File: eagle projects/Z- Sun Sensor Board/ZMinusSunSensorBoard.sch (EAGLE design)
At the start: 194 parts, among them J2 HIROSE_FH19C-6S-0.5SH(10), J3 HIROSE_FH19C-6S-0.5SH(10), J4 HIROSE_FH19C-6S-0.5SH(10), J5 HIROSE_FH19C-6S-0.5SH(10), U1 ADS7841E_2K5, U13 ADS7841E_2K5, U15 TLV9051IDCKR, U19 TLV9051IDCKR, U2 ADS7841E_2K5, U21 TLV9051IDCKR, U23 TLV9051IDCKR, U24 TLV9051IDCKR, U25 ADS7841E_2K5, U26 TLV9051IDCKR, U27 ADS7841E_2K5, U28 TLV9051IDCKR, U29 TLV9051IDCKR, U3 TLV9051IDCKR, U30 TLV9051IDCKR, U31 TLV9051IDCKR, U32 TLV9051IDCKR, U4 LM20BIM7X_NOPB, U6 TLV9051IDCKR, U8 TLV9051IDCKR, U9 TLV9051IDCKR

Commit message: Rev B almost ready
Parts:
- removed A1: XY_SUN_SENSOR, my_library:XY_SUN_SENSOR
- removed C104, C107, C109, C112, C114, C69, C86, C97: 0.1u, resistor:C-EUC0402
- removed C105, C110, C111, C115, C116, C54, C70, C84, C98: 0.022u, resistor:C-EUC0402
- removed C106, C108, C113, C55, C68, C85, C99: 4.7u, resistor:C-EUC0402
- removed J4, J5: HIROSE_FH19C-6S-0.5SH(10), my_library:HIROSE_FH19C-6S-0.5SH(10)
- removed JP1: (no value), pinhead:PINHD-1X2
- removed JP3: (no value), pinhead:PINHD-2X5
- removed R2: 0R, rcl:R-US_R0805
- removed R28, R57, R63, R69: 13.7k, resistor:R-US_R0402
- removed R31, R46, R55, R61, R67: 3.74k, resistor:R-US_R0402
- removed R56, R62, R68: 280R, resistor:R-US_R0402
- removed TP12, TP18, TP20, TP7, TP8: TESTPOINT, my_library:TESTPOINT
- removed U15, U24, U28, U30, U31, U32: TLV9051IDCKR, my_library:TLV9051IDCKR
- added C10, C17, C24, C36, C39, C58, C64, C7: 0.1u, resistor:C-EUC0402
- added C11, C18, C34, C37, C40, C59, C8: 0.022u, resistor:C-EUC0402
- added C13, C23, C35, C38, C44, C57, C6, C63, C9: 4.7u, rcl:C-EUC0805
- added C2: 0.1u, rcl:C-EUC0402
- added J1: TE-1734829-2, my_library:TE-1734829-2
- added JP2, JP4, JP5, JP6: (no value), my_library:PINHD-1X6_MTG_HOLES_MTG
- added R27: 5.1M, rcl:R-US_R0402
- added R30, R37, R43, R49, R71, R79: 280R, resistor:R-US_R0402
- added R35, R41, R72, R74, R80: 13.7k, resistor:R-US_R0402
- added R36, R42, R73, R75, R81: 3.74k, resistor:R-US_R0402
- added TP23, TP24, TP25, TP27, TP29: TESTPOINT, my_library:TESTPOINT
- added U$1: SSR_MOUNT_03, my_library:SSR_MOUNT_03
- added U10, U11, U12, U14, U16, U17: TSV991AILT, my_library:TSV991AILT
- added U5: LM20BIM7X_NOPB, my_library:LM20BIM7X_NOPB
- C100, C71: value 0.022u -> 4.7u; device resistor:C-EUC0402 -> rcl:C-EUC0805
- C101, C27, C32: value 0.022u -> 0.1u
- C103, C96: value 4.7u -> 0.022u
- C25, C28: value 4.7u -> 0.022u; device rcl:C-EUC0805 -> resistor:C-EUC0402
- C26, C29: value 0.1u -> 4.7u; device resistor:C-EUC0402 -> rcl:C-EUC0805
- C52, C82: value 4.7u -> 0.1u
- C53, C67, C83: value 0.1u -> 0.022u
- C87: device resistor:C-EUC0402 -> rcl:C-EUC0805
- J2: value HIROSE_FH19C-6S-0.5SH(10) -> (none); device my_library:HIROSE_FH19C-6S-0.5SH(10) -> my_library:PINHD-2X5_MTG_HOLES
- J3: value HIROSE_FH19C-6S-0.5SH(10) -> (none); device my_library:HIROSE_FH19C-6S-0.5SH(10) -> my_library:HDR_1X2_
- LED1: device led:LEDCHIP-LED0603 -> led:LEDCHIPLED-0603-TTW
- R14, R25: value 280R -> 5.1M; device resistor:R-US_R0402 -> rcl:R-US_R0402
- R15: value 13.7k -> 5.1M; device resistor:R-US_R0402 -> rcl:R-US_R0402
- R17: device resistor:R-US_R0402 -> rcl:R-US_R0402
- R19: value 3.74k -> 5.1M; device resistor:R-US_R0402 -> rcl:R-US_R0402
- R44, R53, R59, R65: value 280R -> 13.7k
- R45, R54, R60, R66: value 13.7k -> 3.74k
- R58, R64, R70: value 3.74k -> 280R
- U19, U21, U23, U26, U29, U3, U6, U8, U9: value TLV9051IDCKR -> TSV991AILT; device my_library:TLV9051IDCKR -> my_library:TSV991AILT
- renumbered C30 to C3, C31 to C4, C33 to C5
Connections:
- removed net !CS!_SUN_Z+: U2.!CS
- removed net N$1: R2.1, U4.VO
- removed net N$13: R14.2, R15.1, U9.+
- removed net N$3: A1G$2.C1, C27.1, R7.1, U6.-
- removed net N$31: R22.2, R23.1, U3.+
- removed net N$34: R25.2, R28.1, U23.+
- removed net N$36: R32.2, R33.1, U24.+
- removed net N$45: R44.2, R45.1, U19.+
- removed net N$47: R50.2, R51.1, U21.+
- removed net N$5: TP17.TP, U25.CH0
- removed net N$56: R56.2, R57.1, U28.+
- removed net N$58: R59.2, R60.1, U29.+
- removed net N$64: R65.2, R66.1, U31.+
- removed net N$66: R68.2, R69.1, U32.+
- removed net N$68: JP3.10
- removed net N$9: R8.2, R9.1, U8.+
- removed net TEMP: R2.2, TP1.TP, U2.CH0
- new net N$20: R27.1, U5.NC
- new net N$27: C8.1, R13.1, U$1G$2.C2, U8.IN-
- new net N$28: R8.2, R9.1, U8.IN+
- new net N$30: R43.2, R44.1, U12.IN+
- new net N$32: R22.2, R23.1, U3.IN+
- new net N$40: R30.2, R35.1, U9.IN+
- new net N$42: C18.1, R42.1, U$1G$2.C1, U11.IN-
- new net N$43: R37.2, R41.1, U11.IN+
- new net N$60: R49.2, R53.1, U14.IN+
- new net N$69: R64.2, R65.1, U23.IN+
- new net N$71: R71.2, R72.1, U17.IN+
- new net N$74: R70.2, R74.1, U26.IN+
- new net N$78: R79.2, R80.1, U29.IN+
- new net TEMP_EXT: TP17.TP, U25.CH0, U5.VO
- new net TEMP_INT: TP1.TP, U2.CH0, U4.VO
- net !CS!_SUN_X+: now also J2.2; no longer JP3.2
- net !CS!_SUN_X-: now also J2.7; no longer JP3.7
- net !CS!_SUN_Y+: now also J2.4; no longer JP3.4
- net !CS!_SUN_Y-: now also J2.9; no longer JP3.9
- net !CS!_SUN_Z-: now also J2.6, U2.!CS; no longer JP3.6
- net +3V3: now also C10.1, C100.1, C101.1, C13.1, C17.1, C2.1, C23.1, C24.1, C27.1, C32.1, C35.1, C36.1, C38.1, C39.1, C44.1, C57.1, C58.1, C6.1, C63.1, C64.1, C7.1, C71.1, C9.1, J1.3V3, J2.10, J3.1, R35.2, R41.2, R44.2, R53.2, R59.2, R65.2, R72.2, R74.2, R80.2, U10.VCC, U11.VCC, U12.VCC, U14.VCC, U16.VCC, U17.VCC, U19.VCC, U21.VCC, U23.VCC, U26.VCC, U29.VCC, U3.VCC, U5.V+, U6.VCC, U8.VCC, U9.VCC; no longer C103.1, C104.1, C106.1, C107.1, C108.1, C109.1, C112.1, C113.1, C114.1, C25.1, C28.1, C53.1, C55.1, C67.1, C68.1, C69.1, C83.1, C85.1, C86.1, C96.1, C97.1, C99.1, JP1.1, R15.2, R28.2, R45.2, R54.2, R57.2, R60.2, R63.2, R66.2, R69.2, U15.V+, U19.V+, U21.V+, U23.V+, U24.V+, U26.V+, U28.V+, U29.V+, U3.V+, U30.V+, U31.V+, U32.V+, U6.V+, U8.V+, U9.V+
- net 0_DEGREES: now also C18.2, R42.2, TP24.TP, U11.OUT; no longer C27.2, R7.2, TP3.TP, U6.OUT
- net 120_DEGREES: now also C8.2; no longer C32.2
- net 240_DEGREES: now also R7.2, TP3.TP, U6.OUT; no longer R19.2, TP8.TP, U9.OUT
- net GND: now also C10.2, C100.2, C101.2, C13.2, C17.2, C2.2, C23.2, C24.2, C27.2, C32.2, C35.2, C36.2, C38.2, C39.2, C44.2, C57.2, C58.2, C6.2, C63.2, C64.2, C7.2, C71.2, C9.2, J1.GND, JP2.2, JP2.4, JP2.6, JP4.2, JP4.4, JP4.6, JP5.2, JP5.4, JP5.6, JP6.2, JP6.4, JP6.6, R15.1, R19.1, R25.2, R27.2, R30.1, R37.1, R43.1, R49.1, R58.1, R64.1, R70.1, R71.1, R79.1, U$1G$2.A1, U$1G$2.A2, U$1G$2.A3, U10.VSS, U11.VSS, U12.VSS, U14.VSS, U16.VSS, U17.VSS, U19.VSS, U21.VSS, U23.VSS, U26.VSS, U29.VSS, U3.VSS, U5.GND_1, U5.GND_2, U6.VSS, U8.VSS, U9.VSS; no longer A1G$2.A1, A1G$2.A2, A1G$2.A3, C103.2, C104.2, C106.2, C107.2, C108.2, C109.2, C112.2, C113.2, C114.2, C25.2, C28.2, C53.2, C55.2, C67.2, C68.2, C69.2, C83.2, C85.2, C86.2, C96.2, C97.2, C99.2, J2.2, J2.4, J2.6, J2.MTGTAB1, J2.MTGTAB2, J3.4, J3.6, J3.MTGTAB1, J3.MTGTAB2, J4.2, J4.4, J4.6, J4.MTGTAB1, J4.MTGTAB2, J5.2, J5.4, J5.6, J5.MTGTAB1, J5.MTGTAB2, JP1.2, R25.1, R44.1, R53.1, R56.1, R59.1, R62.1, R65.1, R68.1, U15.V-, U19.V-, U21.V-, U23.V-, U24.V-, U26.V-, U28.V-, U29.V-, U3.V-, U30.V-, U31.V-, U32.V-, U6.V-, U8.V-, U9.V-
- net N$10: now also R15.2
- net N$11: now also R14.2
- net N$12: now also R7.1, U$1G$2.C3, U6.IN-; no longer A1G$2.C3, R19.1, U9.-
- net N$14: now also R19.2
- net N$23: now also C96.1, JP6.3, R75.1, U26.IN-; no longer C100.1, J5.3, R31.1, U23.-
- net N$29: now also C83.1, JP6.1, R66.1, U23.IN-; no longer C84.1, J5.1, R24.1, U3.-
- net N$35: now also C103.1, JP6.5, R81.1, U29.IN-; no longer C101.1, J5.5, R34.1, U24.-
- net N$37: now also C34.1, JP5.1, R45.1, U12.IN-; no longer C98.1, J4.1, R64.1, U30.-
- net N$38: now also C25.1, JP4.1, U10.IN-; no longer C54.1, J3.1, U15.-
- net N$41: now also R32.2, R33.1, U16.IN+; no longer R38.2, R39.1, U15.+
- net N$44: now also C40.1, JP4.3, R24.1, U3.IN-; no longer C70.1, J3.3, R46.1, U19.-
- net N$46: now also C53.1, JP4.5, R34.1, U16.IN-; no longer C71.1, J3.5, R52.1, U21.-
- net N$49: now also C11.1, JP2.1, R36.1, U9.IN-; no longer C105.1, J2.1, R55.1, U26.-
- net N$54: now also R50.2, R51.1, U19.IN+; no longer R53.2, R54.1, U26.+
- net N$55: now also C28.1, JP2.3, R54.1, U14.IN-; no longer C110.1, J2.3, R58.1, U28.-
- net N$57: now also C37.1, JP2.5, R73.1, U17.IN-; no longer C111.1, J2.5, R61.1, U29.-
- net N$6: now also R38.2, R39.1, U10.IN+; no longer R1.2, R3.1, U6.+
- net N$61: now also R58.2, R59.1, U21.IN+; no longer R62.2, R63.1, U30.+
- net N$63: now also C59.1, JP5.3, R52.1, U19.IN-; no longer C115.1, J4.3, R67.1, U31.-
- net N$65: now also C67.1, JP5.5, R60.1, U21.IN-; no longer C116.1, J4.5, R70.1, U32.-
- net N$67: now also J2.8, R25.1; no longer JP3.8
- net N$8: now also R1.2, R3.1, U6.IN+; no longer A1G$2.C2, C32.1, R13.1, U8.-
- net UCB0_SPI_CLK: now also J2.5; no longer JP3.5
- net UCB0_SPI_MISO: now also J2.1; no longer JP3.1
- net UCB0_SPI_MOSI: now also J2.3; no longer JP3.3
- net X+_0_DEGREES: now also C11.2, R36.2, U9.OUT; no longer C105.2, R55.2, U26.OUT
- net X+_120_DEGREES: now also C28.2, R54.2, TP16.TP, U14.OUT; no longer C110.2, R58.2, TP15.TP, U28.OUT
- net X+_240_DEGREES: now also C37.2, R73.2, TP25.TP, U17.OUT; no longer C111.2, R61.2, TP16.TP, U29.OUT
- net X-_0_DEGREES: now also C25.2, U10.OUT; no longer C54.2, U15.OUT
- net X-_120_DEGREES: now also C40.2, R24.2, TP5.TP, U3.OUT; no longer C70.2, R46.2, TP11.TP, U19.OUT
- net X-_240_DEGREES: now also C53.2, R34.2, TP9.TP, U16.OUT; no longer C71.2, R52.2, TP12.TP, U21.OUT
- net Y+_0_DEGREES: now also C34.2, R45.2, TP11.TP, U12.OUT; no longer C98.2, R64.2, TP18.TP, U30.OUT
- net Y+_120_DEGREES: now also C59.2, R52.2, TP15.TP, U19.OUT; no longer C115.2, R67.2, TP19.TP, U31.OUT
- net Y+_240_DEGREES: now also C67.2, R60.2, TP19.TP, U21.OUT; no longer C116.2, R70.2, TP20.TP, U32.OUT
- net Y-_0_DEGREES: now also C103.2, R81.2, TP29.TP, U29.OUT; no longer C84.2, R24.2, TP5.TP, U3.OUT
- net Y-_120_DEGREES: now also C96.2, R75.2, TP27.TP, U26.OUT; no longer C100.2, R31.2, TP7.TP, U23.OUT
- net Y-_240_DEGREES: now also C83.2, R66.2, TP23.TP, U23.OUT; no longer C101.2, R34.2, TP9.TP, U24.OUT
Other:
- note removed: "Custom machine sun sensor mount for Z- face photodiodes mechanically to board"

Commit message: I thinks its done
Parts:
- JP2, JP4, JP5, JP6: device my_library:PINHD-1X6_MTG_HOLES_MTG -> my_library:PINHD-2X3_MTG_HOLESHOLES
- LED1: device led:LEDCHIPLED-0603-TTW -> led:LEDCHIP-LED0603
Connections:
- net GND: now also JP2.1, JP2.3, JP2.5, JP4.1, JP4.3, JP4.5, JP5.1, JP5.3, JP5.5, JP6.1, JP6.3, JP6.5; no longer JP2.2, JP2.4, JP2.6, JP4.2, JP4.4, JP4.6, JP5.2, JP5.4, JP5.6, JP6.2, JP6.4, JP6.6
- net N$23: now also JP6.4; no longer JP6.3
- net N$29: now also JP6.6; no longer JP6.1
- net N$35: now also JP6.2; no longer JP6.5
- net N$37: now also JP5.2; no longer JP5.1
- net N$38: now also JP4.2; no longer JP4.1
- net N$44: now also JP4.4; no longer JP4.3
- net N$46: now also JP4.6; no longer JP4.5
- net N$49: now also JP2.2; no longer JP2.1
- net N$55: now also JP2.4; no longer JP2.3
- net N$57: now also JP2.6; no longer JP2.5
- net N$63: now also JP5.4; no longer JP5.3
- net N$65: now also JP5.6; no longer JP5.5
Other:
- note added: "ADCS Electrical"
- note added: "B"
- note added: "Temperature Sensors"
- note removed: "A"
- moved on the sheet: JP2, JP4, JP5, JP6

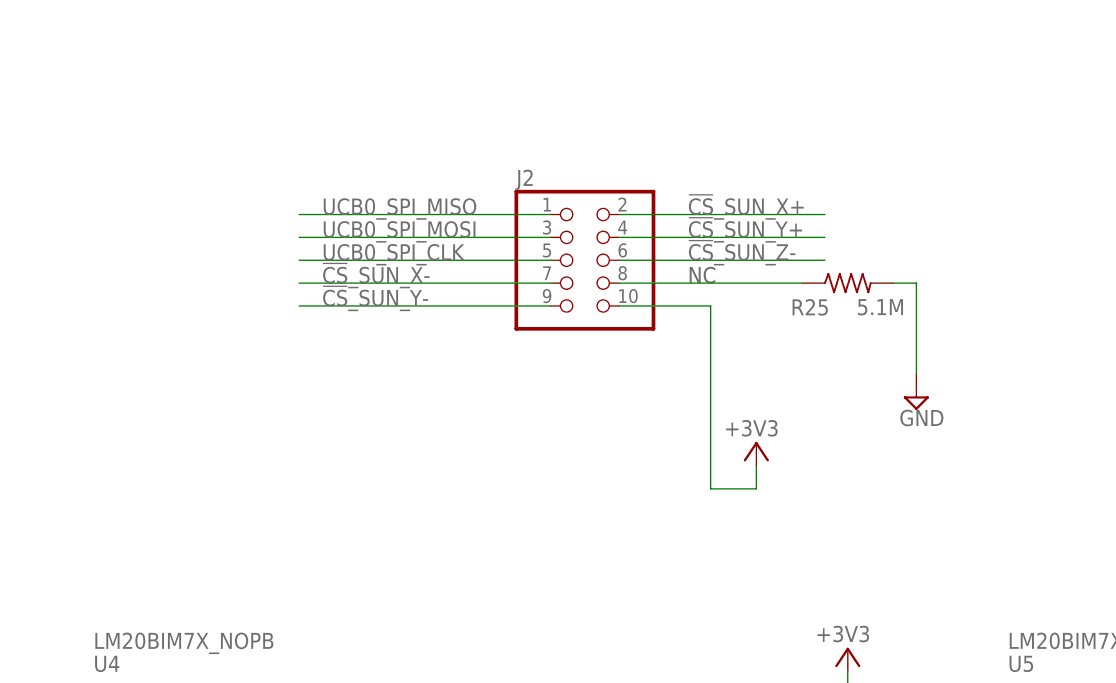
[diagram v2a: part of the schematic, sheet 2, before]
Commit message: Changed most connector changes of Z- board
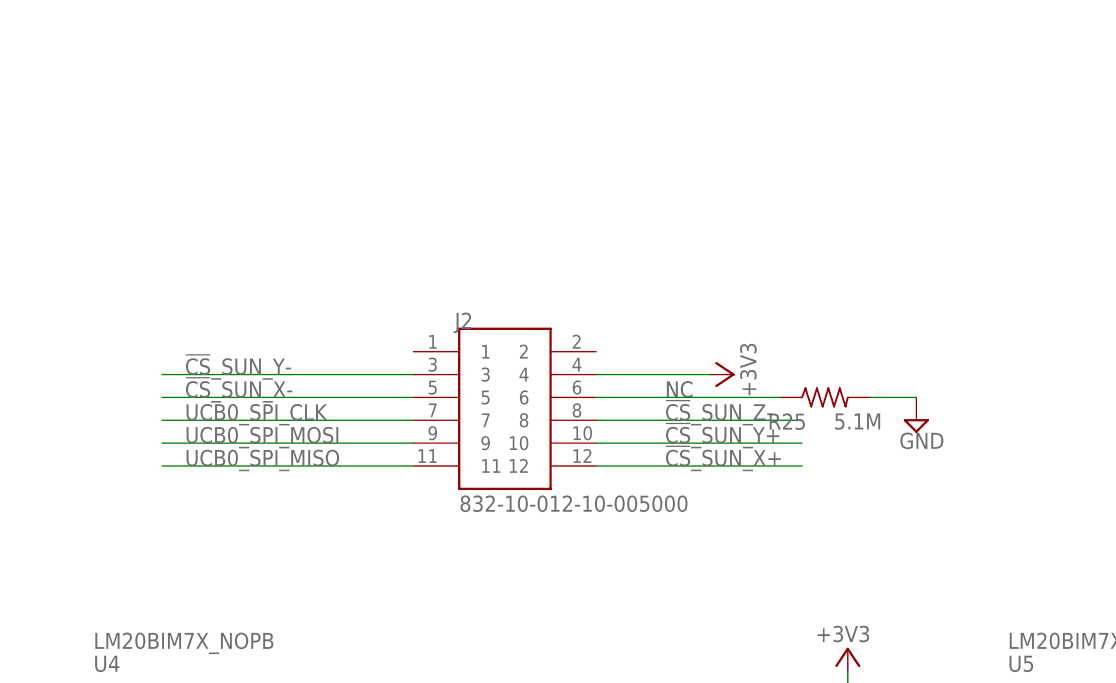
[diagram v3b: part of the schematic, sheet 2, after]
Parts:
- removed JP2, JP4, JP5, JP6: (no value), my_library:PINHD-2X3_MTG_HOLESHOLES
- added J4, J5, J6, J7: 830-10-006-20-005000, 830-10-006-20-005000:830-10-006-20-005000
- J2: value (none) -> 832-10-012-10-005000; device my_library:PINHD-2X5_MTG_HOLES -> 832-10-012-10-005000:832-10-012-10-005000
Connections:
- removed net N$23: C96.1, JP6.4, R75.1, U26.IN-
- removed net N$35: C103.1, JP6.2, R81.1, U29.IN-
- removed net N$37: C34.1, JP5.2, R45.1, U12.IN-
- removed net N$63: C59.1, JP5.4, R52.1, U19.IN-
- new net N$13: C96.1, J7.3, R75.1, U26.IN-
- new net N$17: C103.1, J7.5, R81.1, U29.IN-
- new net N$3: C34.1, J6.5, R45.1, U12.IN-
- new net N$5: C59.1, J6.3, R52.1, U19.IN-
- net !CS!_SUN_X+: now also J2.12; no longer J2.2
- net !CS!_SUN_X-: now also J2.5; no longer J2.7
- net !CS!_SUN_Y+: now also J2.10; no longer J2.4
- net !CS!_SUN_Y-: now also J2.3; no longer J2.9
- net !CS!_SUN_Z-: now also J2.8; no longer J2.6
- net +3V3: now also J2.4; no longer J2.10
- net GND: now also J4.2, J4.4, J4.6, J5.2, J5.4, J5.6, J6.2, J6.4, J6.6, J7.2, J7.4, J7.6; no longer JP2.1, JP2.3, JP2.5, JP4.1, JP4.3, JP4.5, JP5.1, JP5.3, JP5.5, JP6.1, JP6.3, JP6.5
- net N$29: now also J7.1; no longer JP6.6
- net N$38: now also J4.5; no longer JP4.2
- net N$44: now also J4.3; no longer JP4.4
- net N$46: now also J4.1; no longer JP4.6
- net N$49: now also J5.5; no longer JP2.2
- net N$55: now also J5.3; no longer JP2.4
- net N$57: now also J5.1; no longer JP2.6
- net N$65: now also J6.1; no longer JP5.6
- net N$67: now also J2.6; no longer J2.8
- net UCB0_SPI_CLK: now also J2.7; no longer J2.5
- net UCB0_SPI_MISO: now also J2.11; no longer J2.1
- net UCB0_SPI_MOSI: now also J2.9; no longer J2.3
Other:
- moved on the sheet: R25

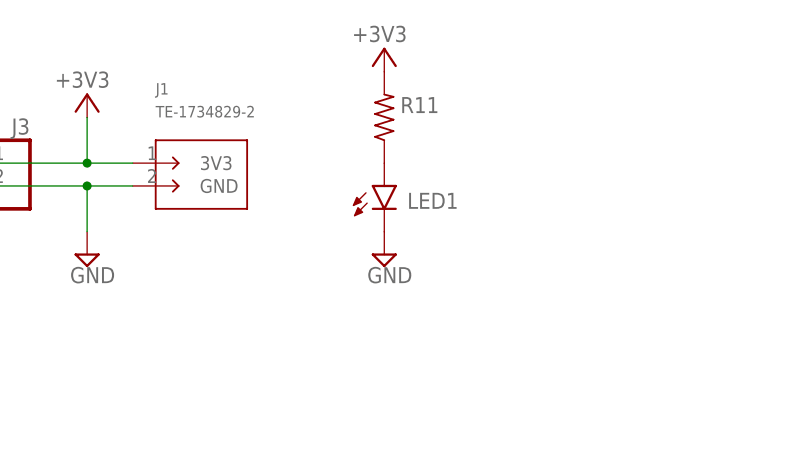
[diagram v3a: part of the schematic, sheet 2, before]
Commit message: Removed LED to Z-
Removed a voltage testing LED and associated resistor from the Z- board, BOM was updated accordingly.
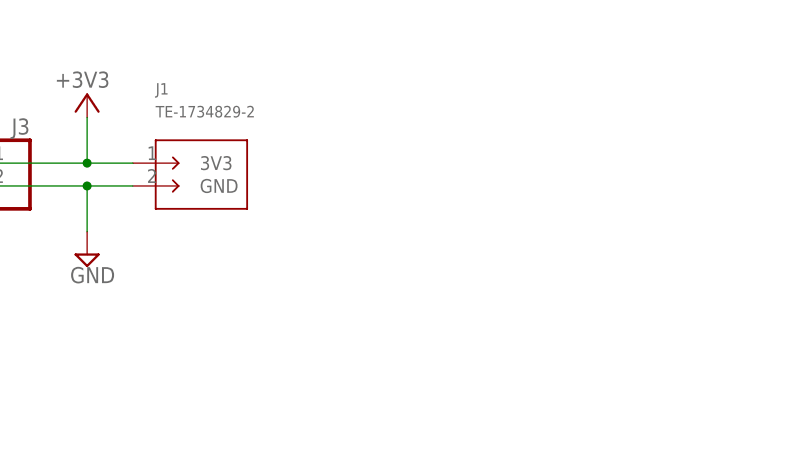
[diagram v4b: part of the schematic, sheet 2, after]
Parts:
- removed LED1: (no value), led:LEDCHIP-LED0603
- removed R11: (no value), rcl:R-US_R0603
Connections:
- removed net N$21: LED1.A, R11.1
- net +3V3: no longer R11.2
- net GND: no longer LED1.C
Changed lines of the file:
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@@
 <part name="J1" library="my_library" library_urn="urn:adsk.eagle:library:22876504" deviceset="TE-1734829-2" device="" package3d_urn="urn:adsk.eagle:package:27602902/2"/>
 <part name="J3" library="my_library" library_urn="urn:adsk.eagle:library:22876504" deviceset="HDR_1X2" device="_" package3d_urn="urn:adsk.eagle:package:24527019/1"/>
-<part name="R11" library="rcl" library_urn="urn:adsk.eagle:library:334" deviceset="R-US_" device="R0603" package3d_urn="urn:adsk.eagle:package:23555/3"/>
-<part name="LED1" library="led" library_urn="urn:adsk.eagle:library:259" deviceset="LED" device="CHIP-LED0603" package3d_urn="urn:adsk.eagle:package:15819/3"/>
-<part name="+3V22" library="supply1" library_urn="urn:adsk.eagle:library:371" deviceset="+3V3" device=""/>
-<part name="SUPPLY1" library="supply2" library_urn="urn:adsk.eagle:library:372" deviceset="GND" device=""/>
 <part name="+3V23" library="supply1" library_urn="urn:adsk.eagle:library:371" deviceset="+3V3" device=""/>
 <part name="SUPPLY9" library="supply2" library_urn="urn:adsk.eagle:library:372" deviceset="GND" device=""/>
@@
 <attribute name="VALUE" x="105.41" y="167.64" size="1.778" layer="96" rot="MR0"/>
 </instance>
-<instance part="R11" gate="G$1" x="144.78" y="180.34" smashed="yes" rot="R90">
-<attribute name="NAME" x="146.558" y="180.8226" size="1.778" layer="95"/>
-<attribute name="VALUE" x="148.082" y="176.53" size="1.778" layer="96" rot="R90"/>
-</instance>
-<instance part="LED1" gate="G$1" x="144.78" y="172.72" smashed="yes">
-<attribute name="NAME" x="147.32" y="170.18" size="1.778" layer="95"/>
-<attribute name="VALUE" x="150.495" y="168.148" size="1.778" layer="96" rot="R90"/>
-</instance>
-<instance part="+3V22" gate="G$1" x="144.78" y="187.96" smashed="yes">
-<attribute name="VALUE" x="147.32" y="190.5" size="1.778" layer="96" rot="R180"/>
-</instance>
-<instance part="SUPPLY1" gate="GND" x="144.78" y="165.1" smashed="yes">
-<attribute name="VALUE" x="142.875" y="161.925" size="1.778" layer="96"/>
-</instance>
 <instance part="+3V23" gate="G$1" x="111.76" y="182.88" smashed="yes">
 <attribute name="VALUE" x="114.3" y="185.42" size="1.778" layer="96" rot="R180"/>
@@
 </segment>
 </net>
-<net name="N$21" class="0">
-<segment>
-<pinref part="R11" gate="G$1" pin="1"/>
-<pinref part="LED1" gate="G$1" pin="A"/>
-</segment>
-</net>
 <net name="+3V3" class="0">
-<segment>
-<pinref part="R11" gate="G$1" pin="2"/>
-<pinref part="+3V22" gate="G$1" pin="+3V3"/>
-</segment>
 <segment>
 <pinref part="J3" gate="G$1" pin="1"/>
@@
 <net name="GND" class="0">
 <segment>
-<pinref part="LED1" gate="G$1" pin="C"/>
-<pinref part="SUPPLY1" gate="GND" pin="GND"/>
-</segment>
-<segment>
 <pinref part="J1" gate="G$1" pin="GND"/>

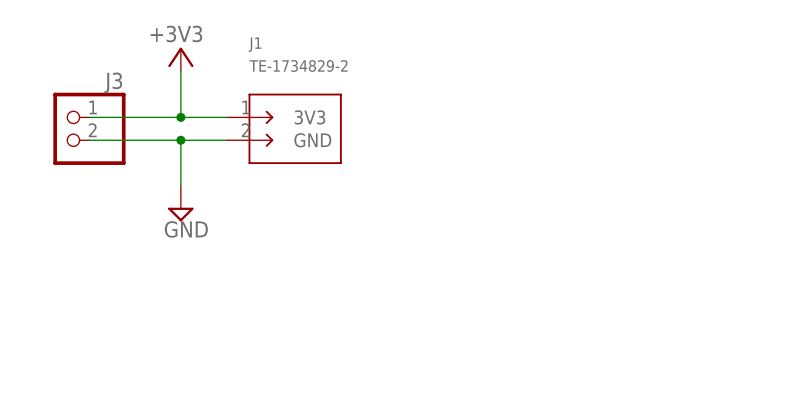
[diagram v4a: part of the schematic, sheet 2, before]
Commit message: Added Luc's recommended new power connectors
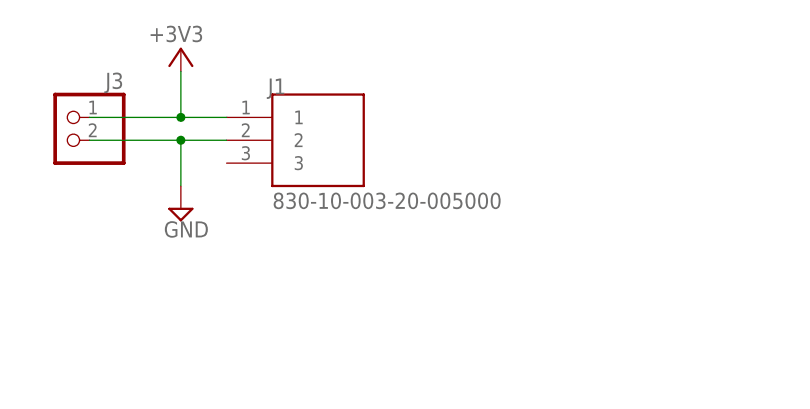
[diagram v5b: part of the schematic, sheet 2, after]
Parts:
- J1: value TE-1734829-2 -> 830-10-003-20-005000; device my_library:TE-1734829-2 -> 830-10-003-20-005000:830-10-003-20-005000
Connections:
- net +3V3: now also J1.1; no longer J1.3V3
- net GND: now also J1.2; no longer J1.GND
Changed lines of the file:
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@@
 <attribute name="REVIEWER" value=""/>
 </part>
-<part name="J1" library="my_library" library_urn="urn:adsk.eagle:library:22876504" deviceset="TE-1734829-2" device="" package3d_urn="urn:adsk.eagle:package:27602902/2"/>
 <part name="J3" library="my_library" library_urn="urn:adsk.eagle:library:22876504" deviceset="HDR_1X2" device="_" package3d_urn="urn:adsk.eagle:package:24527019/1"/>
 <part name="+3V23" library="supply1" library_urn="urn:adsk.eagle:library:371" deviceset="+3V3" device=""/>
@@
 <part name="SUPPLY68" library="supply2" library_urn="urn:adsk.eagle:library:372" deviceset="GND" device=""/>
 <part name="J2" library="832-10-012-10-005000" deviceset="832-10-012-10-005000" device=""/>
+<part name="J1" library="830-10-003-20-005000" deviceset="830-10-003-20-005000" device=""/>
 </parts>
 <sheets>
@@
 <attribute name="REVIEWER" x="196.85" y="6.35" size="2.54" layer="94"/>
 </instance>
-<instance part="J1" gate="G$1" x="121.92" y="175.26" smashed="yes">
-<attribute name="NAME" x="119.38" y="182.88" size="1.27" layer="95"/>
-<attribute name="VALUE" x="119.38" y="180.34" size="1.27" layer="96"/>
-</instance>
 <instance part="J3" gate="G$1" x="99.06" y="172.72" smashed="yes" rot="MR0">
 <attribute name="NAME" x="105.41" y="178.435" size="1.778" layer="95" rot="MR0"/>
@@
 <attribute name="NAME" x="116.34" y="114.3" size="1.778" layer="95"/>
 <attribute name="VALUE" x="116.84" y="93.98" size="1.778" layer="96"/>
+</instance>
+<instance part="J1" gate="G$1" x="127" y="170.18" smashed="yes">
+<attribute name="NAME" x="121.42" y="177.8" size="1.778" layer="95"/>
+<attribute name="VALUE" x="121.92" y="165.1" size="1.778" layer="96"/>
 </instance>
 </instances>
@@
 <segment>
 <pinref part="J3" gate="G$1" pin="1"/>
-<pinref part="J1" gate="G$1" pin="3V3"/>
 <wire x1="101.6" y1="175.26" x2="111.76" y2="175.26" width="0.1524" layer="91"/>
 <pinref part="+3V23" gate="G$1" pin="+3V3"/>
@@
 <wire x1="111.76" y1="175.26" x2="111.76" y2="180.34" width="0.1524" layer="91"/>
 <junction x="111.76" y="175.26"/>
+<pinref part="J1" gate="G$1" pin="1"/>
 </segment>
 <segment>
@@
 <net name="GND" class="0">
 <segment>
-<pinref part="J1" gate="G$1" pin="GND"/>
 <pinref part="J3" gate="G$1" pin="2"/>
 <wire x1="116.84" y1="172.72" x2="111.76" y2="172.72" width="0.1524" layer="91"/>
@@
 <wire x1="111.76" y1="167.64" x2="111.76" y2="172.72" width="0.1524" layer="91"/>
 <junction x="111.76" y="172.72"/>
-</segment>
-<segment>
+<pinref part="J1" gate="G$1" pin="2"/>
+</segment>
+<segment>
